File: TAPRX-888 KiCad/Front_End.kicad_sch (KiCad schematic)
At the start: 40 parts, among them J6 Conn_01x03, J7 Conn_01x03, J8 Conn_01x03, J9 Conn_01x03

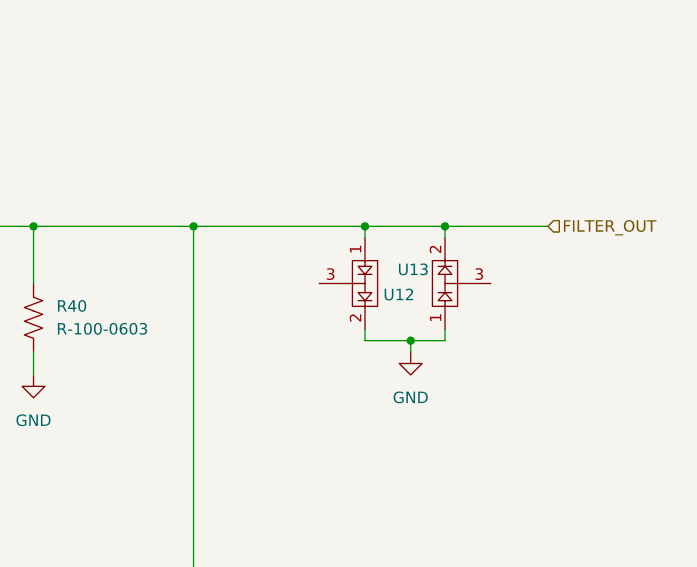
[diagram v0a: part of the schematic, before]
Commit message: acquire Pauls' latest work
in zip file 0.3a.zip.  took its files and put into TAPRX-888 KiCad, renaming them.
Moved old work to a new folder, WB6CXC previous work.
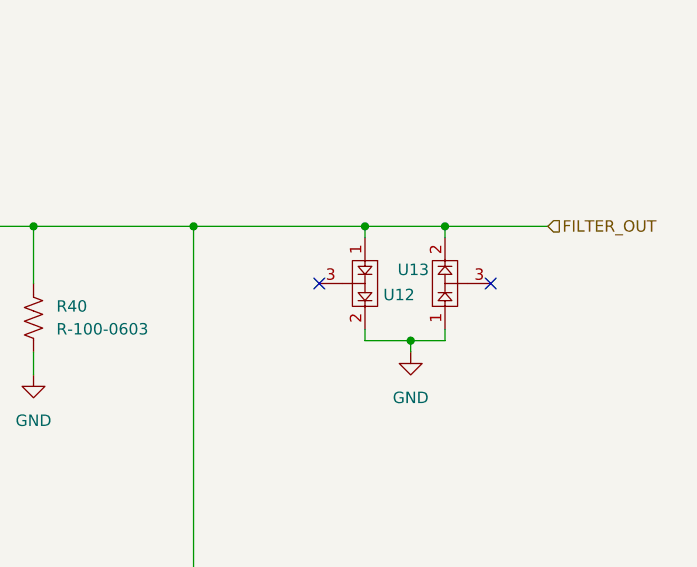
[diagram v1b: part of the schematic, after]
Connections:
- no-connect marks 0 -> 2
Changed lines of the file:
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@@
 		(color 0 0 0 0)
 	)
+	(no_connect
+		(at 238.76 113.03)
+	)
+	(no_connect
+		(at 257.81 113.03)
+	)
 	(wire
 		(pts
@@
 		(pin "2"
 		)
-		(pin "1"
-		)
-		(pin "2"
-		)
 		(instances
 			(project "x-888 v2"
@@
 		(pin "2"
 		)
-		(pin "2"
-		)
-		(pin "1"
-		)
 		(pin "1"
 		)
@@
 		(pin "2"
 		)
-		(pin "2"
-		)
-		(pin "1"
-		)
 		(pin "1"
 		)
@@
 			)
 		)
-		(pin "2"
-		)
-		(pin "1"
-		)
 		(pin "1"
 		)
@@
 			)
 		)
-		(pin "1"
-		)
 		(pin "2"
 		)
 		(pin "1"
 		)
-		(pin "2"
-		)
 		(instances
 			(project "x-888 v2"
@@
 		(pin "1"
 		)
-		(pin "1"
-		)
-		(pin "2"
-		)
 		(instances
 			(project "x-888 v2"
@@
 		(pin "1"
 		)
-		(pin "1"
-		)
-		(pin "2"
-		)
 		(instances
 			(project "x-888 v2"
@@
 		(pin "1"
 		)
-		(pin "1"
-		)
-		(pin "2"
-		)
 		(pin "2"
 		)
@@
 			)
 		)
-		(pin "2"
-		)
-		(pin "1"
-		)
 		(pin "1"
 		)
@@
 		(pin "1"
 		)
-		(pin "1"
-		)
-		(pin "2"
-		)
 		(pin "2"
 		)
@@
 			)
 		)
-		(pin "1"
-		)
-		(pin "2"
-		)
 		(pin "2"
 		)
@@
 			)
 		)
-		(pin "2"
-		)
-		(pin "1"
-		)
 		(pin "1"
 		)
@@
 		(pin "2"
 		)
-		(pin "2"
-		)
-		(pin "1"
-		)
 		(instances
 			(project "x-888 v2"
@@
 		(pin "1"
 		)
-		(pin "1"
-		)
-		(pin "2"
-		)
 		(instances

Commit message: Adding local KiCad symbol and footprint libraries to project
Adding local KiCad symbol and footprint libraries to project
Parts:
- C48, C49: symbol capacitors:C-0.1-0603 -> Library:C-0.1-0603
- C50, C61: symbol capacitors:C-56p-0603 -> Library:C-56p-0603
- C51: symbol capacitors:C-12p-0603 -> Library:C-12p-0603
- C52, C57: symbol capacitors:C-330p-0603 -> Library:C-330p-0603
- C53: symbol capacitors:C-82p-0603 -> Library:C-82p-0603
- C54: symbol capacitors:C-39p-0603 -> Library:C-39p-0603
- C55, C58: symbol capacitors:C-68p-0603 -> Library:C-68p-0603
- C56: symbol capacitors:C-47p-0603 -> Library:C-47p-0603
- C59: symbol capacitors:C-22p-0603 -> Library:C-22p-0603
- C60: symbol capacitors:C-100p-0603 -> Library:C-100p-0603
- J6, J7, J8, J9: symbol TIS:Conn_01x03 -> Library:Conn_01x03
- L10, L11: symbol TIS:Inductor-120n-1008 -> Library:Inductor-120n-1008
- L12, L9: symbol TIS:Inductor-820n-1008 -> Library:Inductor-820n-1008
- L13, L14: symbol TIS:Inductor-150n-1008 -> Library:Inductor-150n-1008
- L8: symbol TIS:Inductor-180n-1008 -> Library:Inductor-180n-1008
- R28, R30, R31, R35, R36, R39: symbol resistors:R-51Ω-0603 -> Library:R-51Ω-0603
- R29, R34: symbol resistors:R-2.2K-0603 -> Library:R-2.2K-0603
- R32, R37: symbol resistors:R-220Ω-0603 -> Library:R-220Ω-0603
- R33, R38: symbol resistors:R-10Ω-0603 -> Library:R-10Ω-0603
- R40: symbol resistors:R-100-0603 -> Library:R-100-0603
- U12, U13: symbol TIS:BAV99-Dual_Diode -> Library:BAV99-Dual_Diode
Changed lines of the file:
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@@
 	)
 	(symbol
-		(lib_id "TIS:GND")
+		(lib_id "Library:GND")
 		(at 76.2 80.01 0)
 		(unit 1)
@@
 	)
 	(symbol
-		(lib_id "resistors:R-10Ω-0603")
+		(lib_id "Library:R-10Ω-0603")
 		(at 116.84 64.77 0)
 		(unit 1)
@@
 	)
 	(symbol
-		(lib_id "capacitors:C-12p-0603")
+		(lib_id "Library:C-12p-0603")
 		(at 64.77 111.76 90)
 		(unit 1)
@@
 	)
 	(symbol
-		(lib_id "TIS:Conn_01x03")
+		(lib_id "Library:Conn_01x03")
 		(at 59.69 21.59 90)
 		(unit 1)
@@
 	)
 	(symbol
-		(lib_id "resistors:R-10Ω-0603")
+		(lib_id "Library:R-10Ω-0603")
 		(at 76.2 64.77 0)
 		(unit 1)
@@
 	)
 	(symbol
-		(lib_id "capacitors:C-68p-0603")
+		(lib_id "Library:C-68p-0603")
 		(at 99.06 134.62 0)
 		(unit 1)
@@
 	)
 	(symbol
-		(lib_id "TIS:Inductor-180n-1008")
+		(lib_id "Library:Inductor-180n-1008")
 		(at 64.77 123.19 0)
 		(unit 1)
@@
 	)
 	(symbol
-		(lib_id "TIS:Inductor-150n-1008")
+		(lib_id "Library:Inductor-150n-1008")
 		(at 170.18 123.19 0)
 		(unit 1)
@@
 	)
 	(symbol
-		(lib_id "TIS:GND")
+		(lib_id "Library:GND")
 		(at 54.61 139.7 0)
 		(unit 1)
@@
 	)
 	(symbol
-		(lib_id "capacitors:C-68p-0603")
+		(lib_id "Library:C-68p-0603")
 		(at 118.11 134.62 0)
 		(unit 1)
@@
 	)
 	(symbol
-		(lib_id "capacitors:C-56p-0603")
+		(lib_id "Library:C-56p-0603")
 		(at 54.61 134.62 0)
 		(unit 1)
@@
 	)
 	(symbol
-		(lib_id "TIS:GND")
+		(lib_id "Library:GND")
 		(at 116.84 80.01 0)
 		(unit 1)
@@
 	)
 	(symbol
-		(lib_id "resistors:R-51Ω-0603")
+		(lib_id "Library:R-51Ω-0603")
 		(at 124.46 58.42 90)
 		(unit 1)
@@
 	)
 	(symbol
-		(lib_id "resistors:R-2.2K-0603")
+		(lib_id "Library:R-2.2K-0603")
 		(at 54.61 158.75 90)
 		(unit 1)
@@
 	)
 	(symbol
-		(lib_id "resistors:R-220Ω-0603")
+		(lib_id "Library:R-220Ω-0603")
 		(at 76.2 49.53 90)
 		(unit 1)
@@
 	)
 	(symbol
-		(lib_id "resistors:R-2.2K-0603")
+		(lib_id "Library:R-2.2K-0603")
 		(at 81.28 158.75 90)
 		(unit 1)
@@
 	)
 	(symbol
-		(lib_id "capacitors:C-39p-0603")
+		(lib_id "Library:C-39p-0603")
 		(at 86.36 111.76 90)
 		(unit 1)
@@
 	)
 	(symbol
-		(lib_id "TIS:Conn_01x03")
+		(lib_id "Library:Conn_01x03")
 		(at 180.34 99.06 270)
 		(mirror x)
@@
 	)
 	(symbol
-		(lib_id "capacitors:C-330p-0603")
+		(lib_id "Library:C-330p-0603")
 		(at 116.84 40.64 90)
 		(unit 1)
@@
 	)
 	(symbol
-		(lib_id "capacitors:C-82p-0603")
+		(lib_id "Library:C-82p-0603")
 		(at 77.47 134.62 0)
 		(unit 1)
@@
 	)
 	(symbol
-		(lib_id "resistors:R-51Ω-0603")
+		(lib_id "Library:R-51Ω-0603")
 		(at 41.91 165.1 0)
 		(unit 1)
@@
 	)
 	(symbol
-		(lib_id "TIS:Inductor-120n-1008")
+		(lib_id "Library:Inductor-120n-1008")
 		(at 86.36 123.19 0)
 		(unit 1)
@@
 	)
 	(symbol
-		(lib_id "TIS:GND")
+		(lib_id "Library:GND")
 		(at 149.86 139.7 0)
 		(unit 1)
@@
 	)
 	(symbol
-		(lib_id "TIS:BAV99-Dual_Diode")
+		(lib_id "Library:BAV99-Dual_Diode")
 		(at 243.84 113.03 270)
 		(unit 1)
@@
 	)
 	(symbol
-		(lib_id "capacitors:C-0.1-0603")
+		(lib_id "Library:C-0.1-0603")
 		(at 33.02 45.72 90)
 		(unit 1)
@@
 	)
 	(symbol
-		(lib_id "TIS:BAV99-Dual_Diode")
+		(lib_id "Library:BAV99-Dual_Diode")
 		(at 252.73 113.03 90)
 		(unit 1)
@@
 	)
 	(symbol
-		(lib_id "TIS:Conn_01x03")
+		(lib_id "Library:Conn_01x03")
 		(at 57.15 99.06 90)
 		(unit 1)
@@
 	)
 	(symbol
-		(lib_id "resistors:R-220Ω-0603")
+		(lib_id "Library:R-220Ω-0603")
 		(at 116.84 49.53 90)
 		(unit 1)
@@
 	)
 	(symbol
-		(lib_id "resistors:R-100-0603")
+		(lib_id "Library:R-100-0603")
 		(at 207.01 116.84 0)
 		(unit 1)
@@
 	)
 	(symbol
-		(lib_id "capacitors:C-22p-0603")
+		(lib_id "Library:C-22p-0603")
 		(at 128.27 111.76 90)
 		(unit 1)
@@
 	)
 	(symbol
-		(lib_id "capacitors:C-0.1-0603")
+		(lib_id "Library:C-0.1-0603")
 		(at 34.29 158.75 90)
 		(unit 1)
@@
 	)
 	(symbol
-		(lib_id "TIS:GND")
+		(lib_id "Library:GND")
 		(at 67.31 171.45 0)
 		(unit 1)
@@
 	)
 	(symbol
-		(lib_id "capacitors:C-47p-0603")
+		(lib_id "Library:C-47p-0603")
 		(at 106.68 111.76 90)
 		(unit 1)
@@
 	)
 	(symbol
-		(lib_id "TIS:GND")
+		(lib_id "Library:GND")
 		(at 118.11 139.7 0)
 		(unit 1)
@@
 	)
 	(symbol
-		(lib_id "TIS:GND")
+		(lib_id "Library:GND")
 		(at 41.91 171.45 0)
 		(unit 1)
@@
 	)
 	(symbol
-		(lib_id "TIS:Inductor-820n-1008")
+		(lib_id "Library:Inductor-820n-1008")
 		(at 76.2 73.66 90)
 		(unit 1)
@@
 	)
 	(symbol
-		(lib_id "TIS:Inductor-820n-1008")
+		(lib_id "Library:Inductor-820n-1008")
 		(at 116.84 73.66 90)
 		(unit 1)
@@
 	)
 	(symbol
-		(lib_id "TIS:GND")
+		(lib_id "Library:GND")
 		(at 207.01 123.19 0)
 		(unit 1)
@@
 	)
 	(symbol
-		(lib_id "TIS:Inductor-150n-1008")
+		(lib_id "Library:Inductor-150n-1008")
 		(at 128.27 123.19 0)
 		(unit 1)
@@
 	)
 	(symbol
-		(lib_id "capacitors:C-100p-0603")
+		(lib_id "Library:C-100p-0603")
 		(at 149.86 134.62 0)
 		(unit 1)
@@
 	)
 	(symbol
-		(lib_id "resistors:R-51Ω-0603")
+		(lib_id "Library:R-51Ω-0603")
 		(at 109.22 58.42 90)
 		(unit 1)
@@
 	)
 	(symbol
-		(lib_id "TIS:Inductor-120n-1008")
+		(lib_id "Library:Inductor-120n-1008")
 		(at 106.68 123.19 0)
 		(unit 1)
@@
 	)
 	(symbol
-		(lib_id "TIS:GND")
+		(lib_id "Library:GND")
 		(at 182.88 138.43 0)
 		(unit 1)
@@
 	)
 	(symbol
-		(lib_id "TIS:GND")
+		(lib_id "Library:GND")
 		(at 248.92 120.65 0)
 		(unit 1)
@@
 	)
 	(symbol
-		(lib_id "resistors:R-51Ω-0603")
+		(lib_id "Library:R-51Ω-0603")
 		(at 68.58 58.42 90)
 		(unit 1)
@@
 	)
 	(symbol
-		(lib_id "resistors:R-51Ω-0603")
+		(lib_id "Library:R-51Ω-0603")
 		(at 83.82 58.42 90)
 		(unit 1)
@@
 	)
 	(symbol
-		(lib_id "TIS:GND")
+		(lib_id "Library:GND")
 		(at 99.06 139.7 0)
 		(unit 1)
@@
 	)
 	(symbol
-		(lib_id "resistors:R-51Ω-0603")
+		(lib_id "Library:R-51Ω-0603")
 		(at 67.31 165.1 0)
 		(unit 1)
@@
 	)
 	(symbol
-		(lib_id "capacitors:C-56p-0603")
+		(lib_id "Library:C-56p-0603")
 		(at 182.88 133.35 0)
 		(unit 1)
@@
 	)
 	(symbol
-		(lib_id "TIS:GND")
+		(lib_id "Library:GND")
 		(at 77.47 139.7 0)
 		(unit 1)
@@
 	)
 	(symbol
-		(lib_id "capacitors:C-330p-0603")
+		(lib_id "Library:C-330p-0603")
 		(at 76.2 40.64 90)
 		(unit 1)
@@
 	)
 	(symbol
-		(lib_id "TIS:Conn_01x03")
+		(lib_id "Library:Conn_01x03")
 		(at 137.16 21.59 270)
 		(mirror x)

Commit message: Updated ADC component data, fixed KiCad v10 zone issue
ADC name and LCSC # updated
KiCad v10 DRC changes - zone overlap and priority check failed (board OK, just DRC issue).  Fixed DRC by merging zones.
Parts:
- U12, U13: value ~ -> (none)
